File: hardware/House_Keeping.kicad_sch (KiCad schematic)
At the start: 4 parts, among them Q7 SI2302DDS-T1-GE3, U15 CD4051BPWR, U16 CD4051BPWR

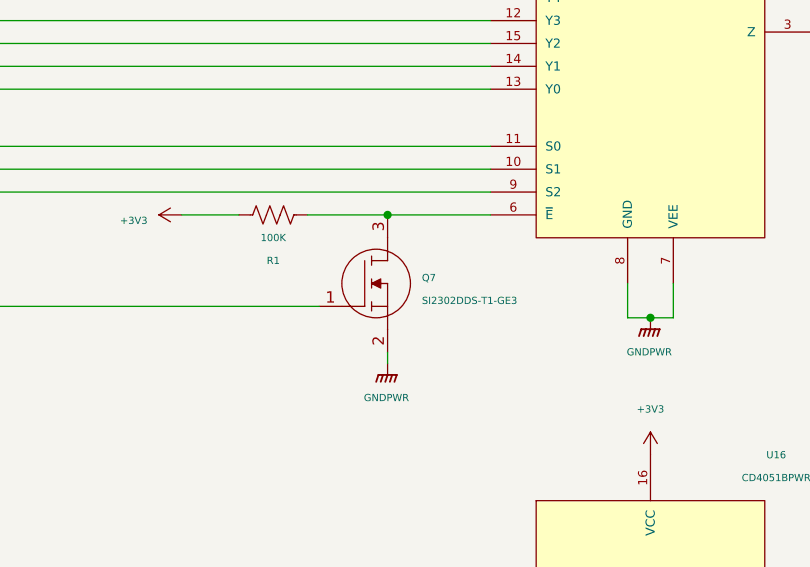
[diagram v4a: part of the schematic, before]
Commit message: hardware: Improving the readability of schematics
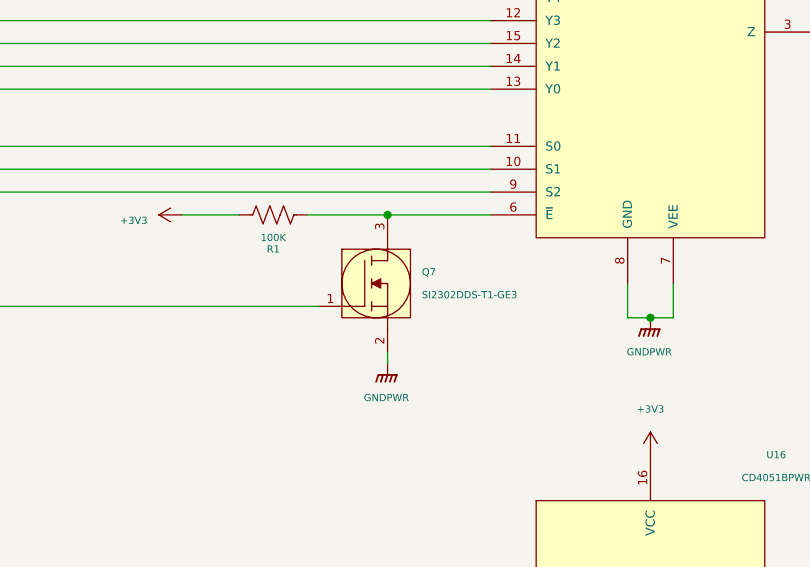
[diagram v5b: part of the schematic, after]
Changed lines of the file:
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@@
   (symbol (lib_id "SI2302DDS-T1-GE3:SI2302DDS-T1-GE3") (at 109.22 105.41 0) (unit 1)
     (in_bom yes) (on_board yes) (dnp no) (fields_autoplaced)
-    (property "Reference" "Q7" (at 120.65 102.235 0)
+    (property "Reference" "Q7" (at 120.65 101.6 0)
       (effects (font (size 0.8 0.8)) (justify left))
     )
-    (property "Value" "SI2302DDS-T1-GE3" (at 120.65 104.775 0)
+    (property "Value" "SI2302DDS-T1-GE3" (at 120.65 104.14 0)
       (effects (font (size 0.8 0.8)) (justify left))
     )
     (property "Footprint" "footprints:SI2302DDS-T1-GE3" (at 97.79 139.7 0)
-      (effects (font (size 0.8 0.8)) (justify left top) hide)
+      (effects (font (size 1.27 1.27)) (justify left top) hide)
     )
     (property "Datasheet" "http://www.vishay.com/docs/63653/si2302dds.pdf" (at 84.836 142.494 0)
-      (effects (font (size 0.8 0.8)) (justify left top) hide)
+      (effects (font (size 1.27 1.27)) (justify left top) hide)
     )
     (property "Height" "1.12" (at 120.65 504.14 0)
-      (effects (font (size 0.8 0.8)) (justify left top) hide)
+      (effects (font (size 1.27 1.27)) (justify left top) hide)
     )
     (property "Mouser Part Number" "78-SI2302DDS-T1-GE3" (at 120.65 604.14 0)
-      (effects (font (size 0.8 0.8)) (justify left top) hide)
+      (effects (font (size 1.27 1.27)) (justify left top) hide)
     )
     (property "Mouser Price/Stock" "https://www.mouser.co.uk/ProductDetail/Vishay-Semiconductors/SI2302DDS-T1-GE3?qs=MxnWX8BLHKdaCSNWhg%252BxLA%3D%3D" (at 120.65 704.14 0)
-      (effects (font (size 0.8 0.8)) (justify left top) hide)
+      (effects (font (size 1.27 1.27)) (justify left top) hide)
     )
     (property "Manufacturer_Name" "Vishay" (at 120.65 804.14 0)
-      (effects (font (size 0.8 0.8)) (justify left top) hide)
+      (effects (font (size 1.27 1.27)) (justify left top) hide)
     )
     (property "Manufacturer_Part_Number" "SI2302DDS-T1-GE3" (at 120.65 904.14 0)
-      (effects (font (size 0.8 0.8)) (justify left top) hide)
+      (effects (font (size 1.27 1.27)) (justify left top) hide)
     )
     (pin "1")
@@
   (symbol (lib_id "CRCW0603100KFKEAHP:CRCW0603100KFKEAHP") (at 110.49 95.25 180) (unit 1)
     (in_bom yes) (on_board yes) (dnp no)
-    (property "Reference" "R1" (at 104.14 100.33 0)
+    (property "Reference" "R1" (at 104.14 99.06 0)
       (effects (font (size 0.8 0.8)))
     )
@@
     )
     (property "Footprint" "footprints:CRCW0603100KFKEAHP" (at 96.52 96.52 0)
-      (effects (font (size 0.8 0.8)) (justify left) hide)
+      (effects (font (size 1.27 1.27)) (justify left) hide)
     )
     (property "Datasheet" "http://uk.rs-online.com/web/p/products/1823583" (at 96.52 93.98 0)
-      (effects (font (size 0.8 0.8)) (justify left) hide)
+      (effects (font (size 1.27 1.27)) (justify left) hide)
     )
     (property "Description" "VISHAY - CRCW0603100KFKEAHP - SMD Chip Resistor, 0603 [1608 Metric], 100 kohm, CRCW-HP e3 Series, 75 V, Thick Film, 250 mW" (at 96.52 91.44 0)
-      (effects (font (size 0.8 0.8)) (justify left) hide)
+      (effects (font (size 1.27 1.27)) (justify left) hide)
     )
     (property "Height" "0.55" (at 96.52 88.9 0)
-      (effects (font (size 0.8 0.8)) (justify left) hide)
+      (effects (font (size 1.27 1.27)) (justify left) hide)
     )
     (property "Manufacturer_Name" "Vishay" (at 96.52 86.36 0)
-      (effects (font (size 0.8 0.8)) (justify left) hide)
+      (effects (font (size 1.27 1.27)) (justify left) hide)
     )
     (property "Manufacturer_Part_Number" "CRCW0603100KFKEAHP" (at 96.52 83.82 0)
-      (effects (font (size 0.8 0.8)) (justify left) hide)
+      (effects (font (size 1.27 1.27)) (justify left) hide)
     )
     (property "Mouser Part Number" "71-CRCW0603100KFKEAH" (at 96.52 81.28 0)
-      (effects (font (size 0.8 0.8)) (justify left) hide)
+      (effects (font (size 1.27 1.27)) (justify left) hide)
     )
     (property "Mouser Price/Stock" "https://www.mouser.co.uk/ProductDetail/Vishay-Dale/CRCW0603100KFKEAHP?qs=niDbCuOAQ0Uxys8g4tQWNQ%3D%3D" (at 96.52 78.74 0)
-      (effects (font (size 0.8 0.8)) (justify left) hide)
+      (effects (font (size 1.27 1.27)) (justify left) hide)
     )
     (property "Arrow Part Number" "CRCW0603100KFKEAHP" (at 96.52 76.2 0)
-      (effects (font (size 0.8 0.8)) (justify left) hide)
+      (effects (font (size 1.27 1.27)) (justify left) hide)
     )
     (property "Arrow Price/Stock" "https://www.arrow.com/en/products/crcw0603100kfkeahp/vishay?region=nac" (at 96.52 73.66 0)
-      (effects (font (size 0.8 0.8)) (justify left) hide)
+      (effects (font (size 1.27 1.27)) (justify left) hide)
     )
     (pin "1")

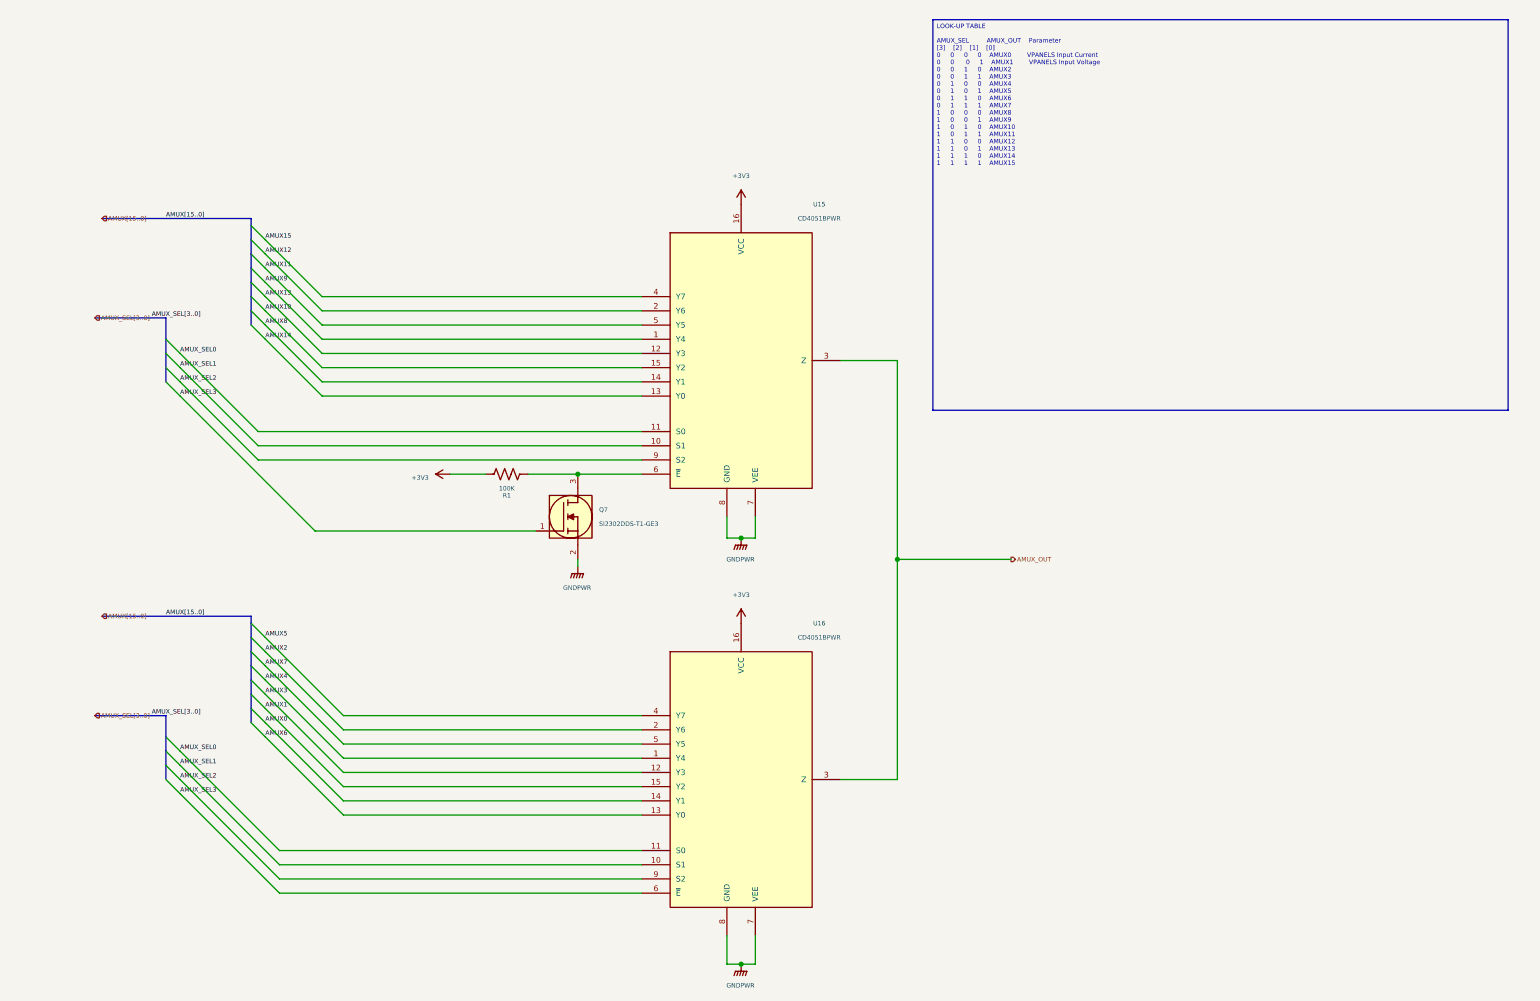
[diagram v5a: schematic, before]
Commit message: hardware: Improving the readability of schematic
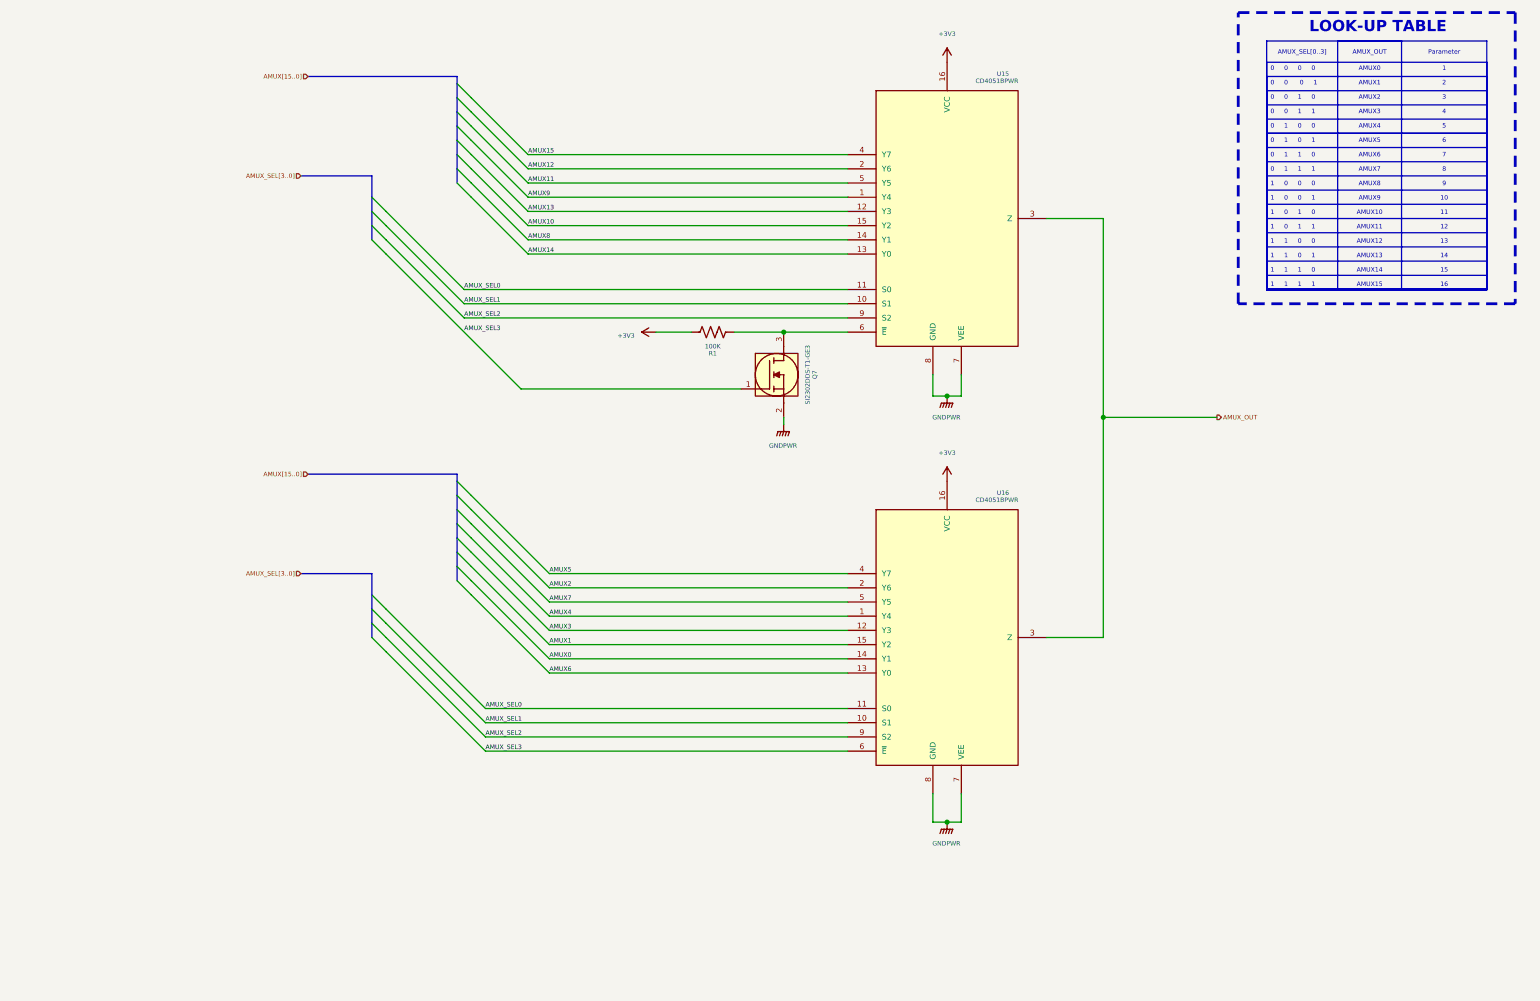
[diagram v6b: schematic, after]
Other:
- note added: "LOOK-UP TABLE"
- moved on the sheet: Q7, R1, U15, U16

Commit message: hardware: Correcting the look-up table and adding an observation regarding improvements
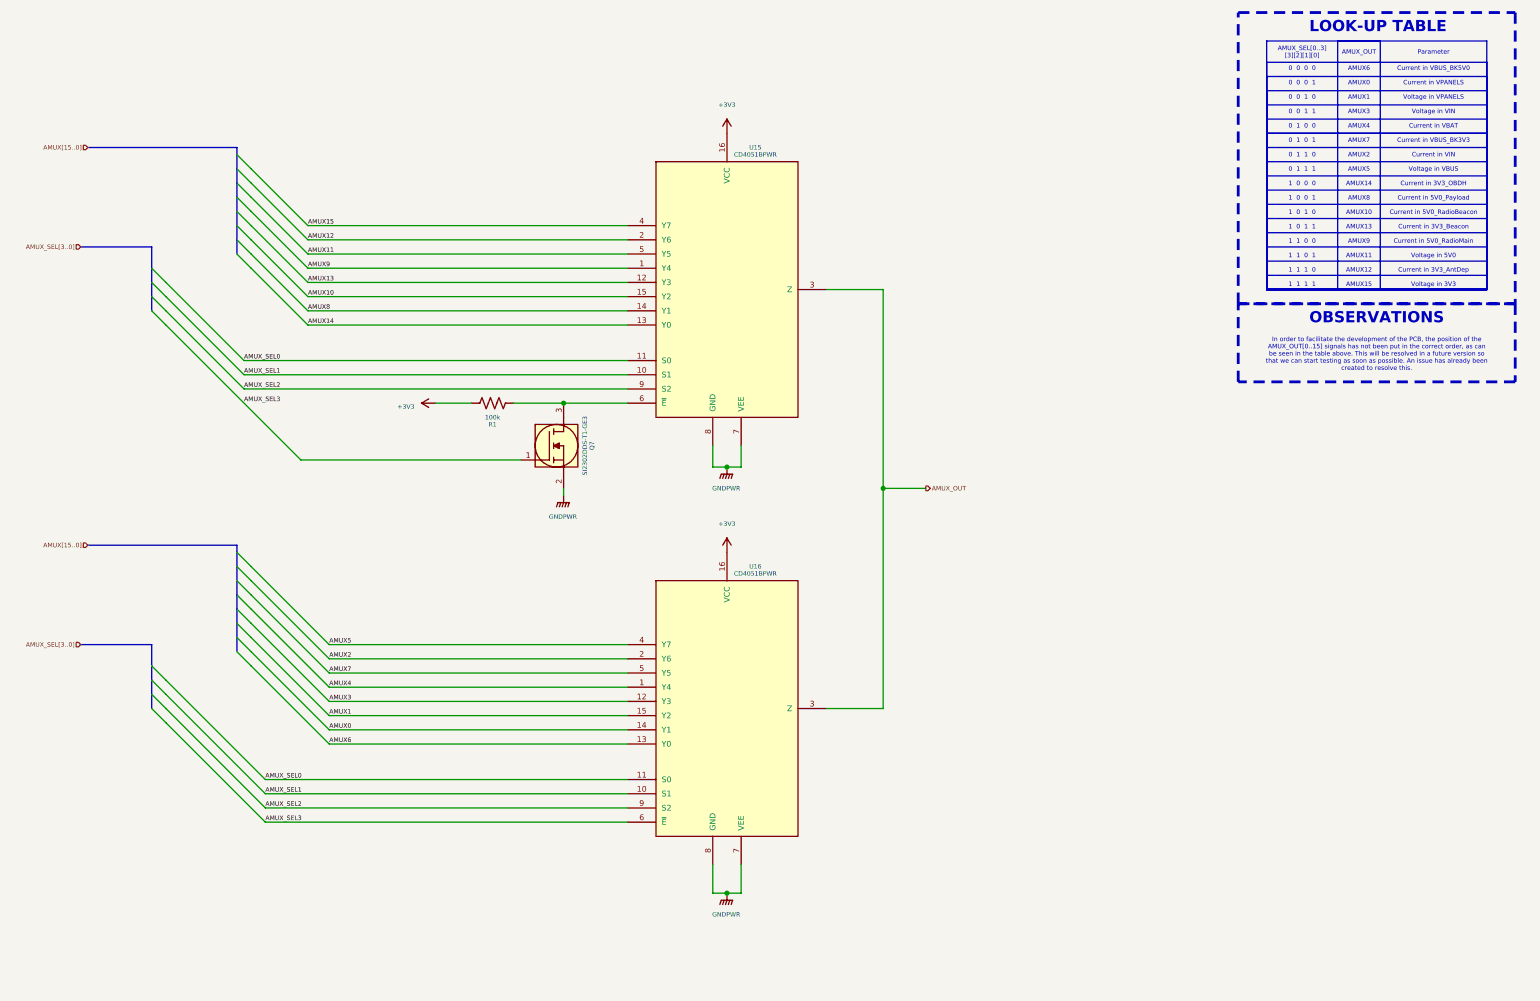
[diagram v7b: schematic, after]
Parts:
- Q7: Height 1.12 -> (none); MPN (none) -> SI2302DDS-T1-GE3; Manufacturer (none) -> Vishay; Manufacturer_Name Vishay -> (none); Manufacturer_Part_Number SI2302DDS-T1-GE3 -> (none); Mouser Part Number 78-SI2302DDS-T1-GE3 -> (none); Mouser Price/Stock https://www.mouser.co.uk/ProductDetail/Vishay-Semiconductor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 -> (none); Package (none) -> SOT-23-3
- R1: value 100K -> 100k; Arrow Part Number CRCW0603100KFKEAHP -> (none); Arrow Price/Stock https://www.arrow.com/en/products/crcw0603100kfkeahp/vishay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 -> (none); Height 0.55 -> (none); MPN (none) -> CRCW0603100KFKEAHP; Manufacturer (none) -> Vishay; Manufacturer_Name Vishay -> (none); Manufacturer_Part_Number CRCW0603100KFKEAHP -> (none); Mouser Part Number 71-CRCW0603100KFKEAH -> (none); Mouser Price/Stock https://www.mouser.co.uk/ProductDetail/Vishay-Dale/CRCW0603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 -> (none); Package (none) -> SMD 0603
- U15, U16: MPN (none) -> CD4051BPWR; Manufacturer (none) -> TI; Package (none) -> TSSOP-16
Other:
- note added: "OBSERVATIONS"
- moved on the sheet: Q7, R1, U15, U16

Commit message: hardware: Minor modifications for the upcoming release
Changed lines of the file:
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@@
     (effects (font (size 0.8 0.8) (color 0 0 0 1)))
   )
-  (text_box "In order to facilitate the development of the PCB, the position of the AMUX_OUT[0..15] signals has not been put in the correct order, as can be seen in the table above. This will be resolved in a future version so that we can start testing as soon as possible. An issue has already been created to resolve this."
+  (text_box "In order to facilitate the development of the PCB, the position of the AMUX_OUT[0..15] signals has not been put in sequence, as can be seen in the table above. This will be resolved in a future version. An issue has already been created to resolve this (issue #21)."
     (at 236.22 68.58 0) (size 46.99 10.16)
     (stroke (width -0.0001) (type default))
